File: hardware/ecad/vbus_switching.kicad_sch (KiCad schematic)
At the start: 0 parts

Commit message: finsihed 6/7 sheets, usb_data needs work. Some warnings to be dealt with aswell but no hard errors.
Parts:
- added C16, C17: 100nF, Capacitor_SMD:C_01005_0402Metric, symbol Device:C
- added C18: 10uF, Capacitor_SMD:C_0603_1608Metric, symbol Device:C
- added R13, R14: 100k, Resistor_SMD:R_0201_0603Metric, symbol Device:R
- added U5: TPS2116DRL, Package_TO_SOT_SMD:SOT-583-8, symbol Power_Management:TPS2116DRL
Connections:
- new net: R13.1, R14.1, U5.4 (PR1)
- new net BOOST_5V: C16.1, R13.2, U5.3 (VIN1)
- new net GND: C16.2, C17.2, C18.2, R14.2, U5.1 (GND)
- new net MODE_SEL: U5.5 (MODE)
- new net VBUS_IN: C17.1, U5.6 (VIN2)
- new net VBUS_KBD: C18.1, U5.2 (VOUT), U5.7 (VOUT)
- no-connect marks 0 -> 1
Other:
- company: (none) -> āvega systems
- title: (none) -> midi2BLE_VBUS_Switching

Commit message: Updated schematics and added printed pdf
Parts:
- C16, C17: footprint Capacitor_SMD:C_01005_0402Metric -> Capacitor_SMD:C_0402_1005Metric
- R13, R14: footprint Resistor_SMD:R_0201_0603Metric -> Capacitor_SMD:C_0402_1005Metric
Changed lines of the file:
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@@
 			)
 		)
-		(property "Footprint" "Resistor_SMD:R_0201_0603Metric"
+		(property "Footprint" "Capacitor_SMD:C_0402_1005Metric"
 			(at 115.57 68.072 90)
 			(hide yes)
@@
 			)
 		)
-		(property "Footprint" "Resistor_SMD:R_0201_0603Metric"
+		(property "Footprint" "Capacitor_SMD:C_0402_1005Metric"
 			(at 104.14 70.612 90)
 			(hide yes)
@@
 			)
 		)
-		(property "Footprint" "Capacitor_SMD:C_01005_0402Metric"
+		(property "Footprint" "Capacitor_SMD:C_0402_1005Metric"
 			(at 172.72 98.0948 0)
 			(hide yes)
@@
 			)
 		)
-		(property "Footprint" "Capacitor_SMD:C_01005_0402Metric"
+		(property "Footprint" "Capacitor_SMD:C_0402_1005Metric"
 			(at 172.72 53.6448 0)
 			(hide yes)

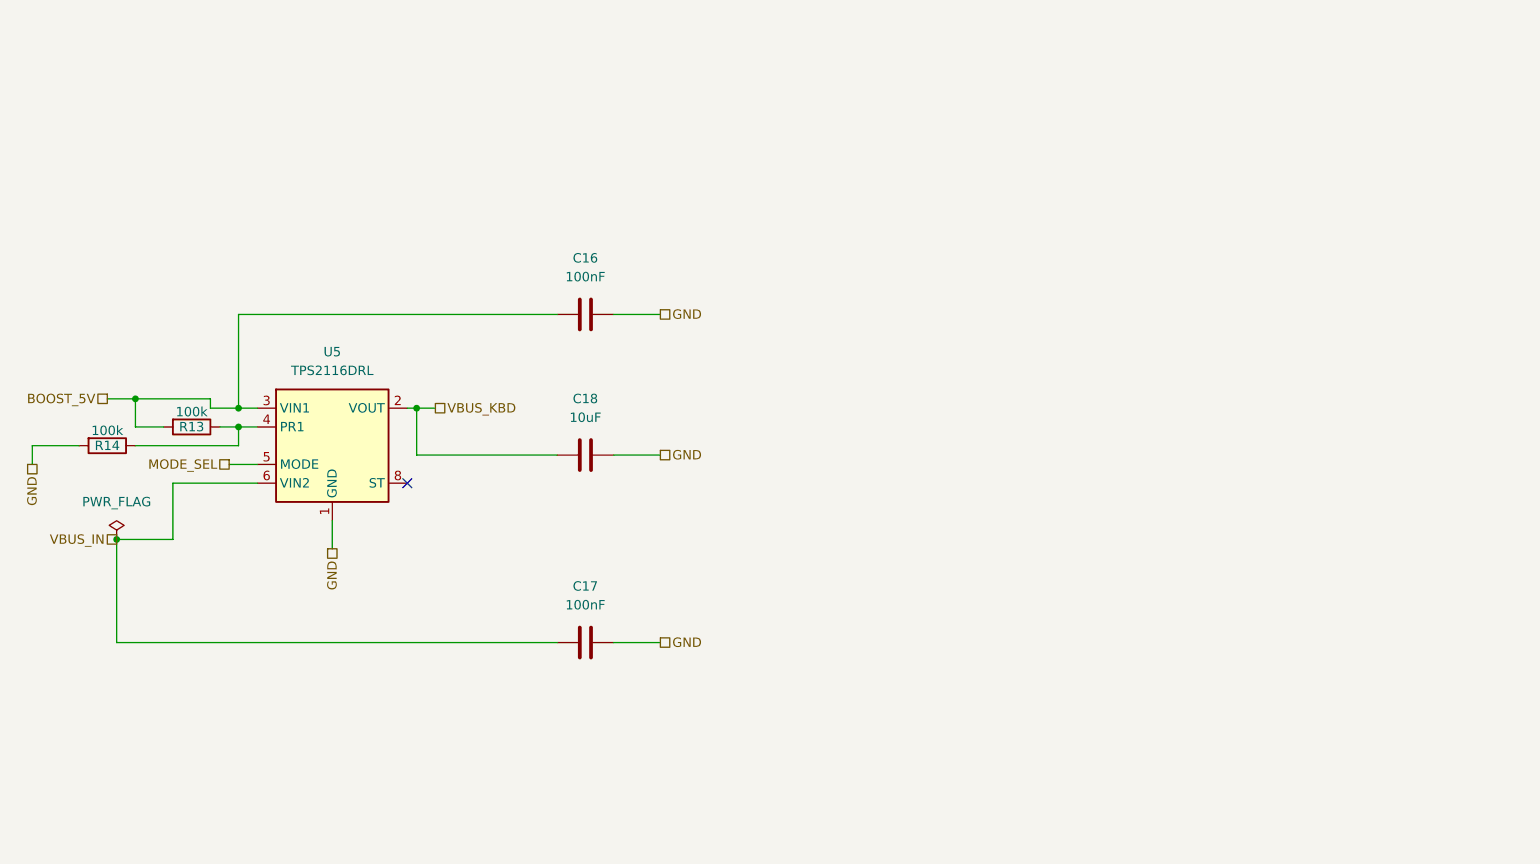
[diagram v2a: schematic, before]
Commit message: fix: resolve fatal power and USB switching errors
Replace TLV61047 boost converter with MT3608; add SS14 catch diode, 4.7µH inductor, and correct FB divider (180kΩ/51kΩ) for 5V output
Fix TPS62162DSG EN circular dependency; connect directly to U1_OUT
Fix TPS62162DSG FB pin; disconnect from SYS_3V3 and tie to GND
Fix TPS2116 power mux; remove series resistor on VIN1, add correct PR1 divider (100kΩ/27kΩ), tie MODE to VIN1 for priority mode
Fix TS3USB30E OE pin; tie directly to GND to keep switch always enabled
Add PGOOD pull-up resistor (10kΩ) to SYS_3V3 on BQ24079
Change ISET resistor from 590Ω to 680Ω for 1.3A charge current
Remove unnecessary R5 (10kΩ VBUS_IN to GND bleed resistor)
Add USB_STATUS net from TPS2116 ST pin to ESP32 IO38
Add PWR_FLAG to BOOST_5V and U1_OUT nets
Fix U1_PGOOD net label placement; separate from SYS_3V3 pull-up node
Add documentation boxes and truth tables to power and USB switching pages
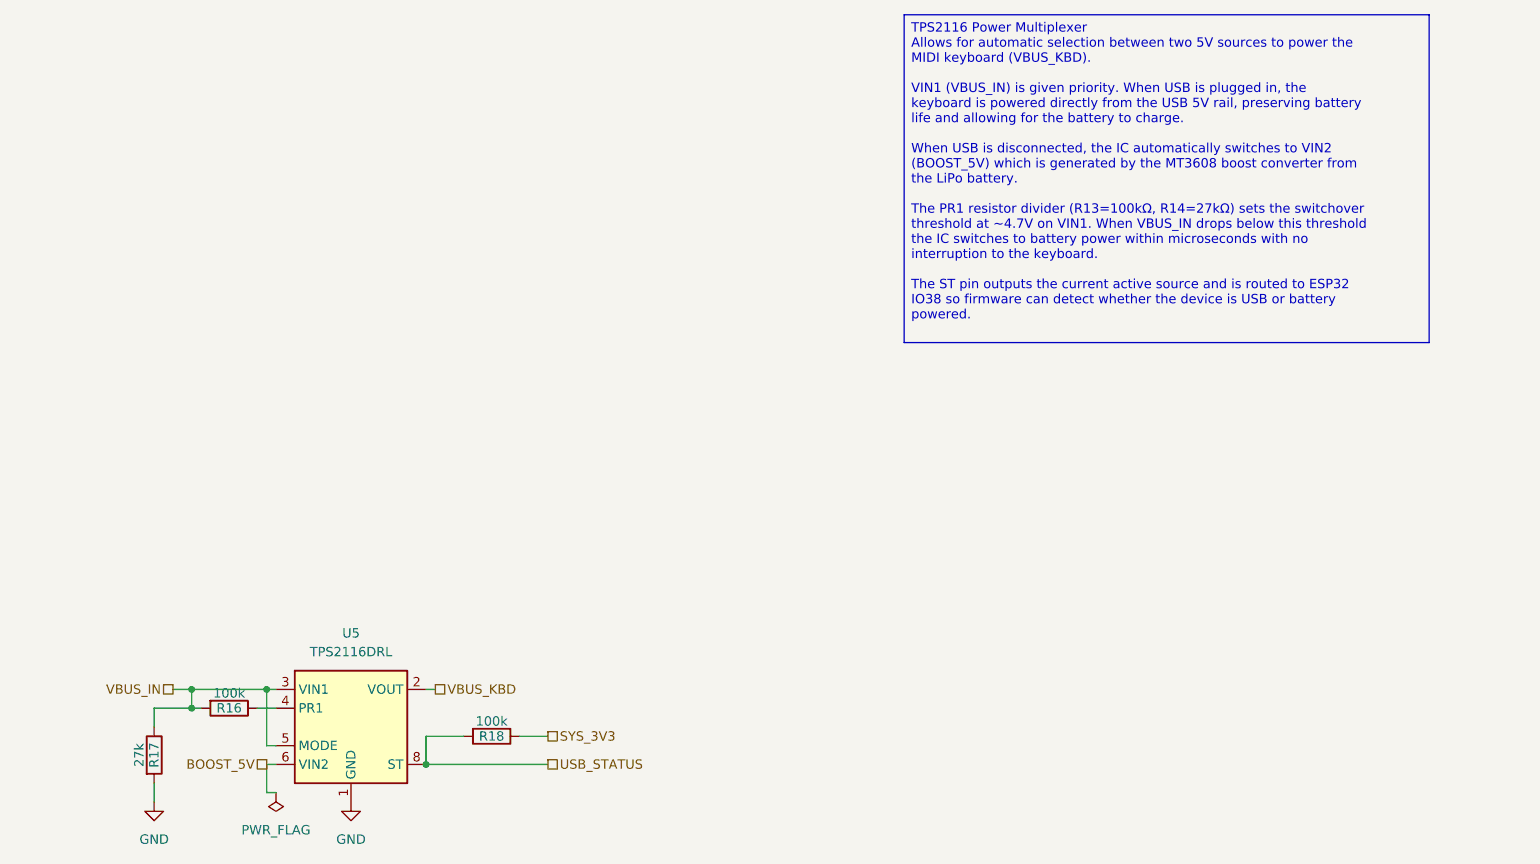
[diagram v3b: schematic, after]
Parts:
- removed C16, C17: 100nF, Capacitor_SMD:C_0402_1005Metric, symbol Device:C
- removed C18: 10uF, Capacitor_SMD:C_0603_1608Metric, symbol Device:C
- removed R13, R14: 100k, Capacitor_SMD:C_0402_1005Metric, symbol Device:R
- added R16, R18: 100k, Capacitor_SMD:C_0402_1005Metric, symbol Device:R
- added R17: 27k, Capacitor_SMD:C_0402_1005Metric, symbol Device:R
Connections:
- net MODE_SEL is gone; now on net VBUS_IN: U5.5 (MODE)
- net BOOST_5V: now also U5.6 (VIN2); no longer U5.3 (VIN1)
- net GND: now also R17.2
- net VBUS_IN: now also U5.3 (VIN1), R16.2, R17.1; no longer U5.6 (VIN2)
- net at U5.4 (PR1): now also R16.1
- net USB_STATUS: now reaches U5.8 (ST)
- net USB_STATUS: now also R18.2
- new net SYS_3V3: R18.1
- no-connect marks 1 -> 0
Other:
- moved on the sheet: U5

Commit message: Fixed minor errors and smaller issues withing schematics, moved v1 pcb and specific projet artifacts to archive. Produced PDF of full schematic
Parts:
- R16, R17, R18: footprint Capacitor_SMD:C_0402_1005Metric -> Resistor_SMD:R_0603_1608Metric
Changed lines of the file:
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@@
 	(title_block
 		(title "midi2BLE_VBUS_Switching")
-		(date "2026-04-13")
-		(rev "1")
+		(date "2026-05-16")
+		(rev "2")
 		(company "āvega systems")
 	)
@@
 			)
 		)
-		(property "Footprint" "Capacitor_SMD:C_0402_1005Metric"
+		(property "Footprint" "Resistor_SMD:R_0603_1608Metric"
 			(at 120.65 106.172 90)
 			(hide yes)
@@
 			)
 		)
-		(property "Footprint" "Capacitor_SMD:C_0402_1005Metric"
+		(property "Footprint" "Resistor_SMD:R_0603_1608Metric"
 			(at 108.712 114.3 90)
 			(hide yes)
@@
 			)
 		)
-		(property "Footprint" "Capacitor_SMD:C_0402_1005Metric"
+		(property "Footprint" "Resistor_SMD:R_0603_1608Metric"
 			(at 156.21 109.982 90)
 			(hide yes)
